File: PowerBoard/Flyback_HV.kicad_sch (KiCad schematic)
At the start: 34 parts, among them J3 Molex Microfit 3.0, Q2 IRL520NSTRLPBF, Q3 FGH75T65SQD-F155, T1 DA2034, U2 LT3750, U4 MCP14A0454-E/SN

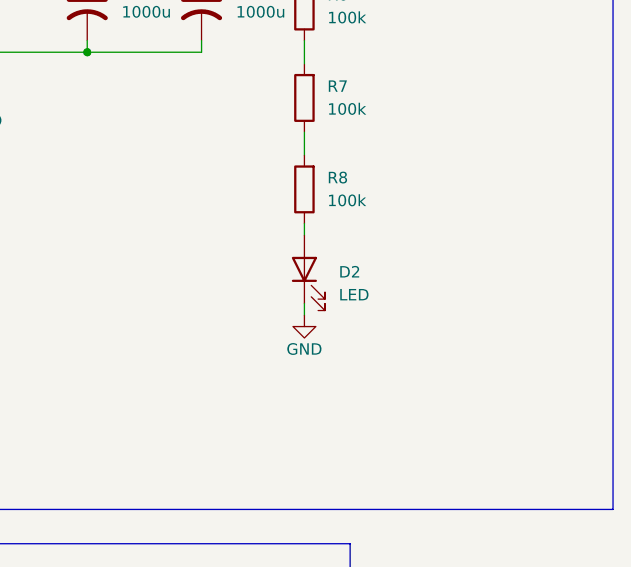
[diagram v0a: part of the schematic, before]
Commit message: updated small details + LEDS
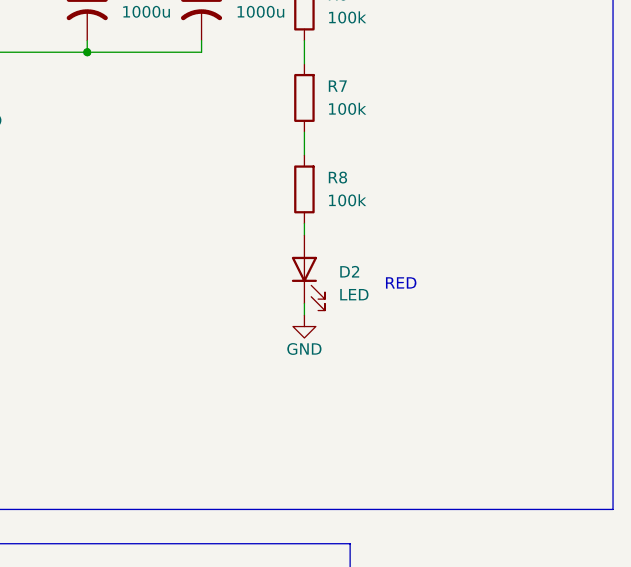
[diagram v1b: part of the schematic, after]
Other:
- note added: "RED"
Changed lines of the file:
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@@
     (effects (font (size 1.27 1.27)) (justify left bottom))
+  )
+  (text "RED" (at 209.55 81.28 0)
+    (effects (font (size 1.27 1.27) (color 255 0 6 1)) (justify left bottom))
   )
   (text "CHICKER CIRCUIT" (at 44.45 111.76 0)
@@
       (effects (font (size 1.27 1.27)) hide)
     )
-    (property "Datasheet" "~" (at 200.66 78.74 0)
-      (effects (font (size 1.27 1.27)) hide)
-    )
+    (property "Datasheet" "APT3216LSECK/J3-PRV" (at 200.66 78.74 0)
+      (effects (font (size 1.27 1.27)) hide)
+    )

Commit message: update to layout
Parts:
- removed C2, C7, C9: 56u, Capacitor_SMD:C_0805_2012Metric, symbol Device:C
- added C10: 0.1u, bots:C_0603_1608Metric, symbol Device:C
- added C27: 1500p, bots:C_0805_2012Metric, symbol Device:C
- added C5 (x3): 100u, Capacitor_SMD:CP_Elec_6.3x5.4_Nichicon, symbol Device:C_Polarized_US
- added D3: D_Schottky, bots:D_SMC, symbol Device:D_Schottky
- added D4: D_Zener, bots:D_SMA, symbol Device:D_Zener
- added J3: Molex Microfit 3.0, bots:Molex_Micro-Fit_3.0_43650-0215_1x02_P3.00mm_Vertical, symbol Connector_Generic:Conn_01x02
- added Q3: FGH75T65SQD-F155, bots:TO-247-3_Horizontal_TabDown, symbol Transistor_IGBT:IRG4PF50W
- added R10: 10k, bots:R_0603_1608Metric, symbol Device:R
- added R29: 2, bots:R_0805_2012Metric, symbol Device:R
- added R9: 110, bots:R_0603_1608Metric, symbol Device:R
- C1, C27, C4: footprint Capacitor_SMD:C_0805_2012Metric -> bots:C_0805_2012Metric
- C10, C3, C8: footprint Capacitor_SMD:C_0603_1608Metric -> bots:C_0603_1608Metric
- D1: footprint Diode_SMD:D_SMB -> bots:D_SMB
- D2: footprint LED_SMD:LED_1206_3216Metric -> bots:LED_1206_3216Metric
- D3: footprint Diode_SMD:D_SMC -> bots:D_SMC
- D4: footprint Diode_SMD:D_SMA -> bots:D_SMA
- J3: footprint bots:Molex_Micro-Fit_3.0_43650-0200_1x02_P3.00mm_Horizontal -> bots:Molex_Micro-Fit_3.0_43650-0215_1x02_P3.00mm_Vertical
- Q2: footprint Package_TO_SOT_SMD:TO-263-2 -> bots:TO-263-2
- R1, R10, R2, R3, R5, R6, R7, R8, R9: footprint Resistor_SMD:R_0603_1608Metric -> bots:R_0603_1608Metric
- R29: footprint Resistor_SMD:R_0805_2012Metric -> bots:R_0805_2012Metric
- R4: footprint Resistor_SMD:R_1206_3216Metric -> bots:R_1206_3216Metric
- U2: footprint Package_SO:MSOP-10_3x3mm_P0.5mm -> bots:MSOP-10_3x3mm_P0.5mm
- U4: footprint SOIC8_SN_MCH -> bots:SOIC-8_3.9x4.9mm_P1.27mm
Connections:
- net GND: no longer C1.2, C10.2, C27.2, C3.2, C4.2, C5.2, C6.2, C8.2, D2.1 (K), D4.2 (A), Q3.3 (E), R10.2, R4.1, R5.1, T1.1 (SB), U2.5 (GND)
- net HV: now also J3.2 (Pin_2), D3.1 (K), J3.2 (Pin_2); no longer J3.1 (Pin_1)
- net VCC: now also C5.1, C5.1, C5.1
- net IGBTGATE_CHICKER: now reaches C10.1, D4.1 (K), Q3.1 (G), R9.1
- net CHICKER_HV: now reaches D3.2 (A), Q3.2 (C), R29.1
- net CHICKER_HV: now also J3.1 (Pin_1); no longer J3.2 (Pin_2)
- net VSOURCE: now reaches Q2.3 (S), R4.2, U2.6 (SOURCE)
- net CHIP_EXTRA: now reaches U4.4 (INB)
- net EXTRA_GATE: now reaches U4.7 (OUTB)
- net EXTRA_GATE: now also R10.1, R9.2
- new net EXTRA_HV: D3.2 (A), J3.1 (Pin_1), Q3.2 (C), R29.1
- new net GNDPWR: C1.2, C10.2, C10.2, C27.2, C27.2, C3.2, C4.2, C5.2, C5.2, C5.2, C5.2, C6.2, C8.2, D2.1 (K), D4.2 (A), D4.2 (A), Q3.3 (E), Q3.3 (E), R10.2, R10.2, R4.1, R5.1, T1.1 (SB), U2.5 (GND)
- new net IGBTGATE_EXTRA: C10.1, D4.1 (K), Q3.1 (G), R9.1
- new net SNUB: C27.1, R29.2
- no-connect marks 3 -> 2
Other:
- note added: "(240-1.8)/2mA"
- note added: "4775.207283"
- note added: "4797.333031"
- note added: "7087.375394"
- note added: "EXTRA REDUNDANCY CHIP"
- moved on the sheet: C1, C10, C27, C3, C4, C5, C6, C8, D1, D2, D3, D4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

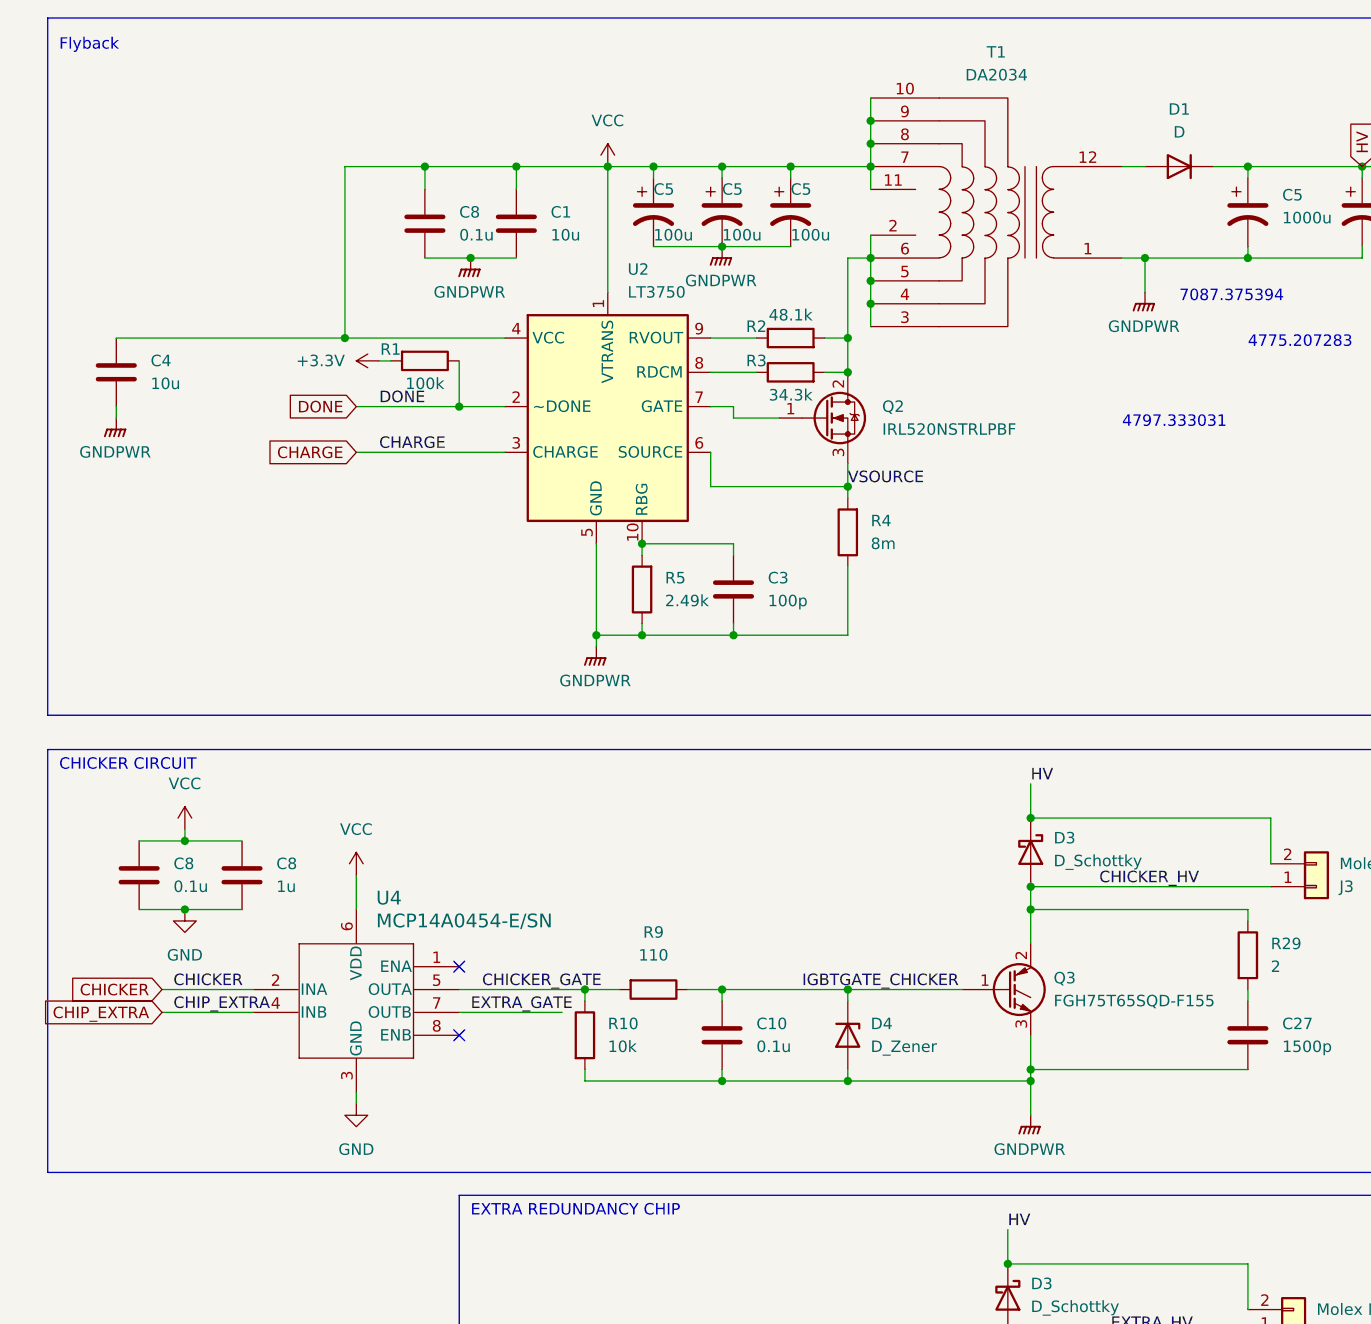
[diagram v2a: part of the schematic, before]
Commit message: layout v1 complete
- consider adding a auto discharge circuit
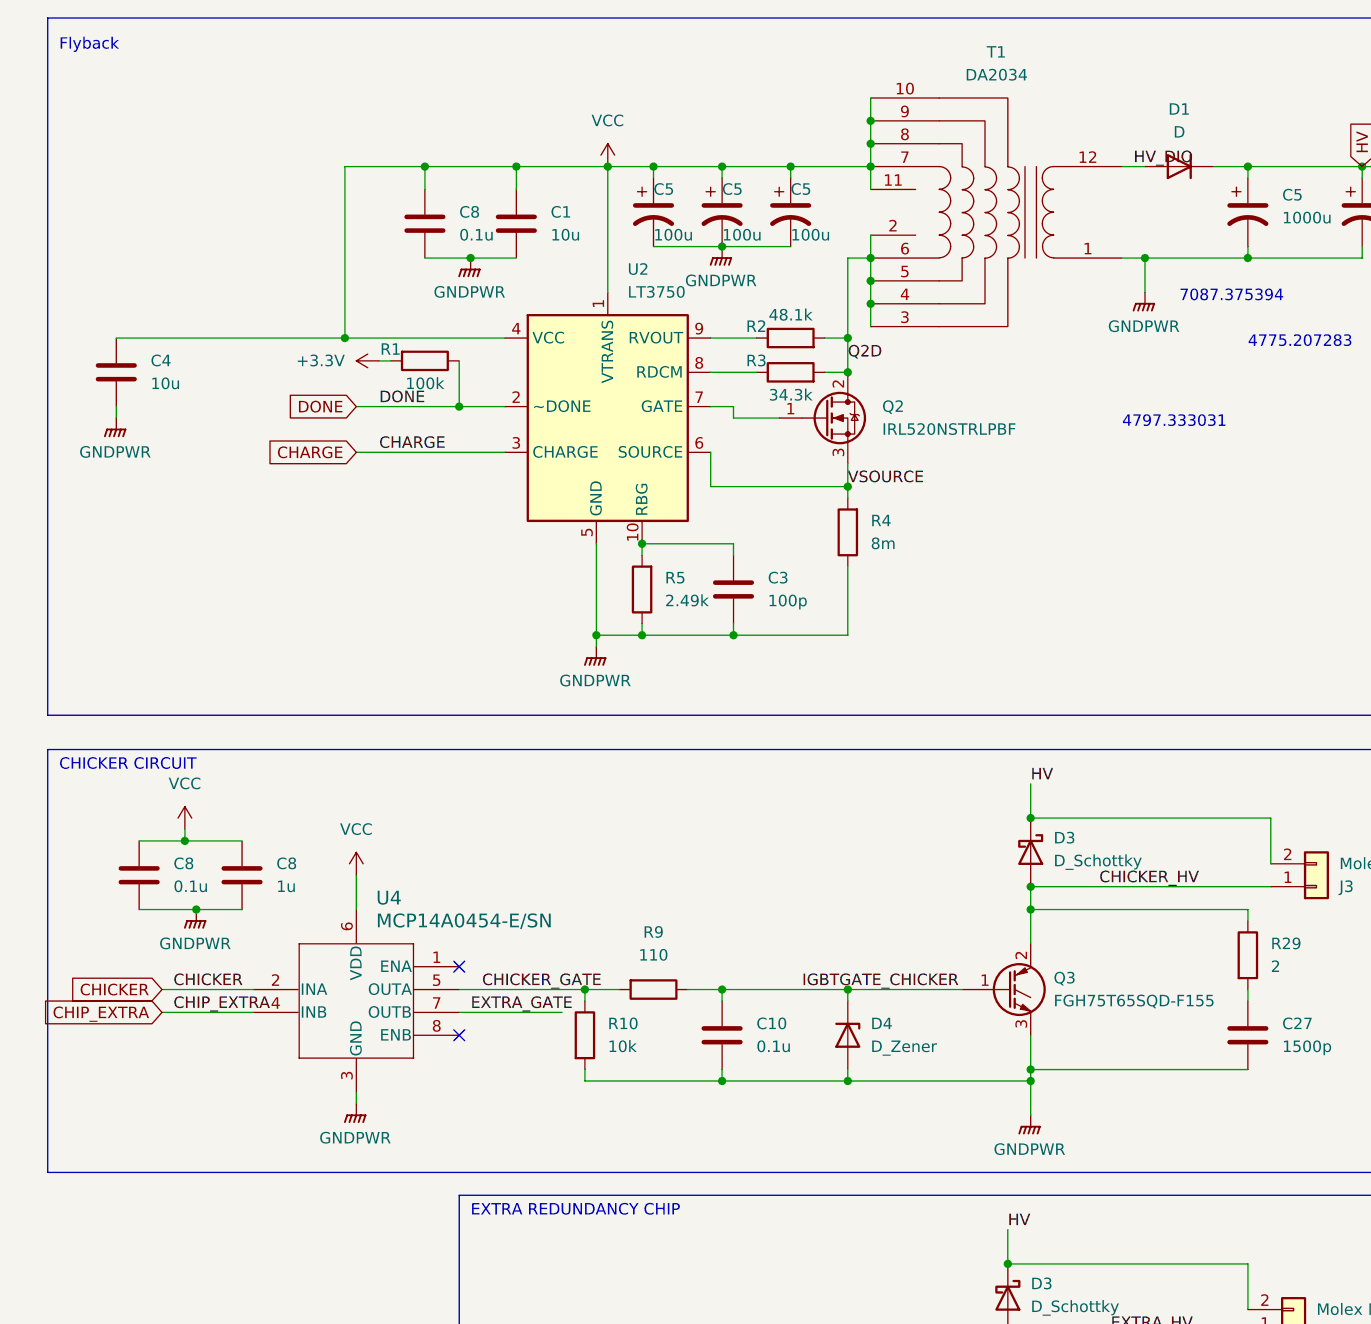
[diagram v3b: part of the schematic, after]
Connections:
- net GND is gone; now on net GNDPWR: C8.2, C8.2, U4.3 (GND)
- net HV_DIO: now reaches D1.2 (A), T1.12 (SB)
- net Q2D: now reaches Q2.2 (D), R2.2, R3.2, T1.2 (AA), T1.3 (AB), T1.4 (AB), T1.5 (AB), T1.6 (AA)
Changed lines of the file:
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@@
   (junction (at 91.44 83.82) (diameter 0) (color 0 0 0 0)
   )
+  (junction (at 31.75 114.3) (diameter 0) (color 0 0 0 0)
+  )
   (junction (at 104.14 50.8) (diameter 0) (color 0 0 0 0)
   )
   (junction (at 106.68 41.91) (diameter 0) (color 0 0 0 0)
-  )
-  (junction (at 30.48 114.3) (diameter 0) (color 0 0 0 0)
   )
   (junction (at 124.46 132.08) (diameter 0) (color 0 0 0 0)
@@
     (stroke (width 0) (type default))
   )
-  (wire (pts (xy 30.48 114.3) (xy 36.83 114.3))
+  (wire (pts (xy 25.4 114.3) (xy 31.75 114.3))
     (stroke (width 0) (type default))
   )
@@
     (stroke (width 0) (type default))
   )
-  (wire (pts (xy 25.4 114.3) (xy 30.48 114.3))
-    (stroke (width 0) (type default))
-  )
   (wire (pts (xy 148.59 31.75) (xy 161.29 31.75))
     (stroke (width 0) (type default))
   )
   (wire (pts (xy 67.31 31.75) (xy 67.31 34.29))
+    (stroke (width 0) (type default))
+  )
+  (wire (pts (xy 31.75 114.3) (xy 36.83 114.3))
     (stroke (width 0) (type default))
   )
@@
   )
   (label "CHICKER_HV" (at 132.08 111.76 0) (fields_autoplaced)
+    (effects (font (size 1.27 1.27)) (justify left bottom))
+  )
+  (label "HV_DIO" (at 135.89 31.75 0) (fields_autoplaced)
+    (effects (font (size 1.27 1.27)) (justify left bottom))
+  )
+  (label "Q2D" (at 104.14 53.34 0) (fields_autoplaced)
     (effects (font (size 1.27 1.27)) (justify left bottom))
   )
@@
         (path "/1a9ce3e8-a091-496c-9c5f-e7b2eb60e275/aa68550e-c35d-4fef-b4e5-f1eb6225215f"
           (reference "Q7") (unit 1)
-        )
-      )
-    )
-  )
-  (symbol (lib_id "power:GND") (at 30.48 114.3 0) (unit 1)
-    (in_bom yes) (on_board yes) (dnp no) (fields_autoplaced)
-    (property "Reference" "#PWR021" (at 30.48 120.65 0)
-      (effects (font (size 1.27 1.27)) hide)
-    )
-    (property "Value" "GND" (at 30.48 119.38 0)
-      (effects (font (size 1.27 1.27)))
-    )
-    (property "Footprint" "" (at 30.48 114.3 0)
-      (effects (font (size 1.27 1.27)) hide)
-    )
-    (property "Datasheet" "" (at 30.48 114.3 0)
-      (effects (font (size 1.27 1.27)) hide)
-    )
-    (pin "1")
-    (instances
-      (project "POWER_BOARD"
-        (path "/1a9ce3e8-a091-496c-9c5f-e7b2eb60e275"
-          (reference "#PWR021") (unit 1)
-        )
-        (path "/1a9ce3e8-a091-496c-9c5f-e7b2eb60e275/aa68550e-c35d-4fef-b4e5-f1eb6225215f"
-          (reference "#PWR062") (unit 1)
         )
       )
@@
     )
   )
+  (symbol (lib_id "power:GNDPWR") (at 31.75 114.3 0) (unit 1)
+    (in_bom yes) (on_board yes) (dnp no) (fields_autoplaced)
+    (property "Reference" "#PWR046" (at 31.75 119.38 0)
+      (effects (font (size 1.27 1.27)) hide)
+    )
+    (property "Value" "GNDPWR" (at 31.623 118.11 0)
+      (effects (font (size 1.27 1.27)))
+    )
+    (property "Footprint" "" (at 31.75 115.57 0)
+      (effects (font (size 1.27 1.27)) hide)
+    )
+    (property "Datasheet" "" (at 31.75 115.57 0)
+      (effects (font (size 1.27 1.27)) hide)
+    )
+    (pin "1")
+    (instances
+      (project "POWER_BOARD"
+        (path "/1a9ce3e8-a091-496c-9c5f-e7b2eb60e275/aa68550e-c35d-4fef-b4e5-f1eb6225215f"
+          (reference "#PWR046") (unit 1)
+        )
+      )
+    )
+  )
   (symbol (lib_id "Device:D_Zener") (at 101.6 177.8 270) (unit 1)
     (in_bom yes) (on_board yes) (dnp no) (fields_autoplaced)
@@
         (path "/1a9ce3e8-a091-496c-9c5f-e7b2eb60e275/aa68550e-c35d-4fef-b4e5-f1eb6225215f"
           (reference "D3") (unit 1)
+        )
+      )
+    )
+  )
+  (symbol (lib_id "power:GNDPWR") (at 49.53 135.89 0) (unit 1)
+    (in_bom yes) (on_board yes) (dnp no) (fields_autoplaced)
+    (property "Reference" "#PWR04" (at 49.53 140.97 0)
+      (effects (font (size 1.27 1.27)) hide)
+    )
+    (property "Value" "GNDPWR" (at 49.403 139.7 0)
+      (effects (font (size 1.27 1.27)))
+    )
+    (property "Footprint" "" (at 49.53 137.16 0)
+      (effects (font (size 1.27 1.27)) hide)
+    )
+    (property "Datasheet" "" (at 49.53 137.16 0)
+      (effects (font (size 1.27 1.27)) hide)
+    )
+    (pin "1")
+    (instances
+      (project "POWER_BOARD"
+        (path "/1a9ce3e8-a091-496c-9c5f-e7b2eb60e275/aa68550e-c35d-4fef-b4e5-f1eb6225215f"
+          (reference "#PWR04") (unit 1)
         )
       )
@@
         )
       )
-    )
-  )
-  (symbol (lib_id "power:GND") (at 49.53 135.89 0) (unit 1)
-    (in_bom yes) (on_board yes) (dnp no) (fields_autoplaced)
-    (property "Reference" "#PWR021" (at 49.53 142.24 0)
-      (effects (font (size 1.27 1.27)) hide)
-    )
-    (property "Value" "GND" (at 49.53 140.97 0)
-      (effects (font (size 1.27 1.27)))
-    )
-    (property "Footprint" "" (at 49.53 135.89 0)
-      (effects (font (size 1.27 1.27)) hide)
-    )
-    (property "Datasheet" "" (at 49.53 135.89 0)
-      (effects (font (size 1.27 1.27)) hide)
-    )
-    (pin "1")
-    (instances
-      (project "POWER_BOARD"
-        (path "/1a9ce3e8-a091-496c-9c5f-e7b2eb60e275"
-          (reference "#PWR021") (unit 1)
-        )
-        (path "/1a9ce3e8-a091-496c-9c5f-e7b2eb60e275/aa68550e-c35d-4fef-b4e5-f1eb6225215f"
-          (reference "#PWR04") (unit 1)
-        )
-      )

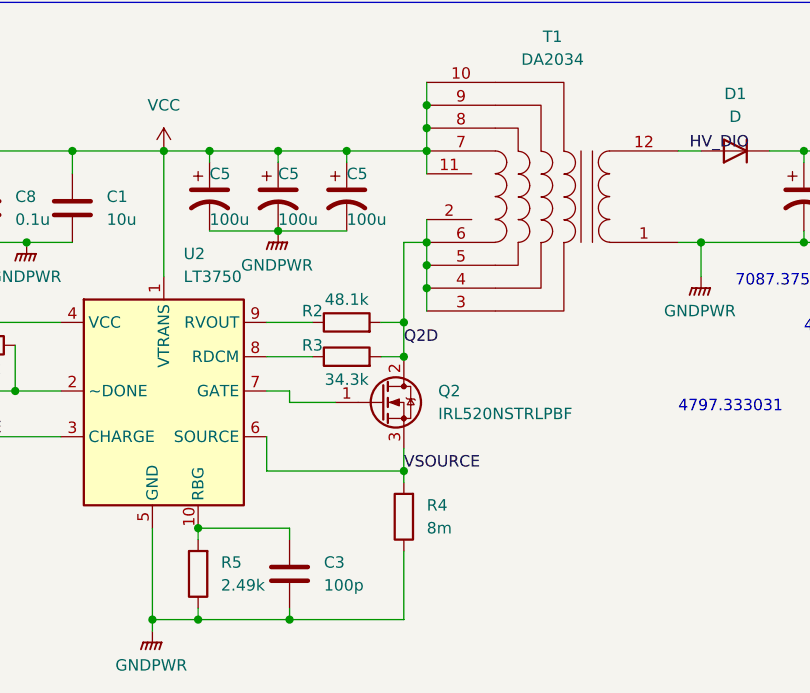
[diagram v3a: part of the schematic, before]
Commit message: updated layout
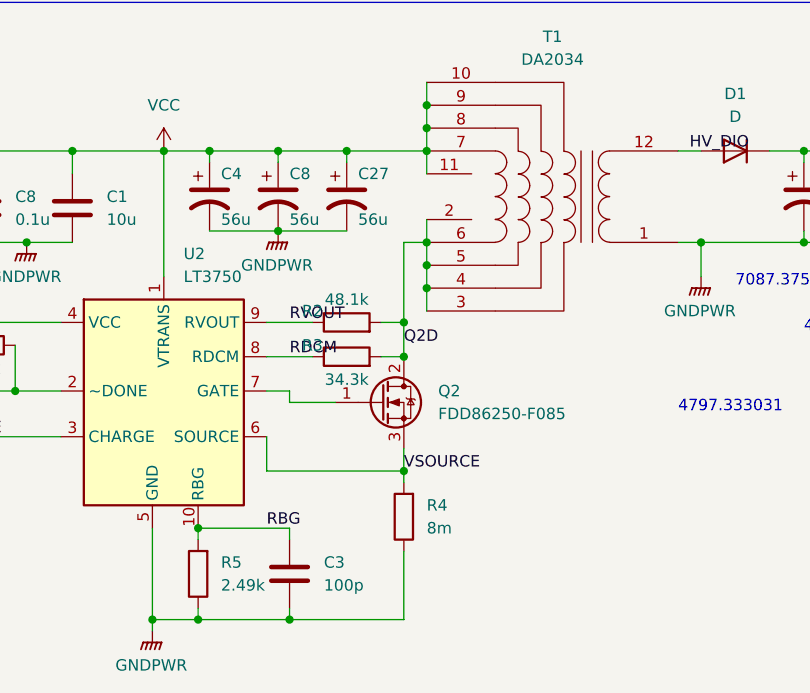
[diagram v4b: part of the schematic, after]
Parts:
- removed C5 (x3): 100u, Capacitor_SMD:CP_Elec_6.3x5.4_Nichicon, symbol Device:C_Polarized_US
- removed Q2: IRL520NSTRLPBF, bots:TO-263-2, symbol Transistor_FET:IRFS4127
- added C27, C4, C8: 56u, bots:CP_Elec_6.3x5.7, symbol bots:CAP_A768EB566M1VLAE042
- added Q2: FDD86250-F085, bots:DPAK-3_ONS, symbol bots:FDD86250-F085
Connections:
- net GNDPWR: now also C27.2, C4.2, C8.2
- net Q2D: now also Q2.2 (D)
- net VCC: now also C27.1, C4.1, C8.1
- net VSOURCE: now also Q2.3 (S)
- net RBG: now reaches C3.1, R5.2, U2.10 (RBG)
- net RVOUT: now reaches R2.1, U2.9 (RVOUT)
- net at U2.7 (GATE): now also Q2.1 (G)
- net RDCM: now reaches R3.1, U2.8 (RDCM)
